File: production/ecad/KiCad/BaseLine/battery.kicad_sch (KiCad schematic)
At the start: 22 parts, among them IC1 AP7362-33SP-13 (3.3V LDO), J3 Conn_01x02, Q3 Si3456DDV, U5 LTC3872ETS8TRMPBF

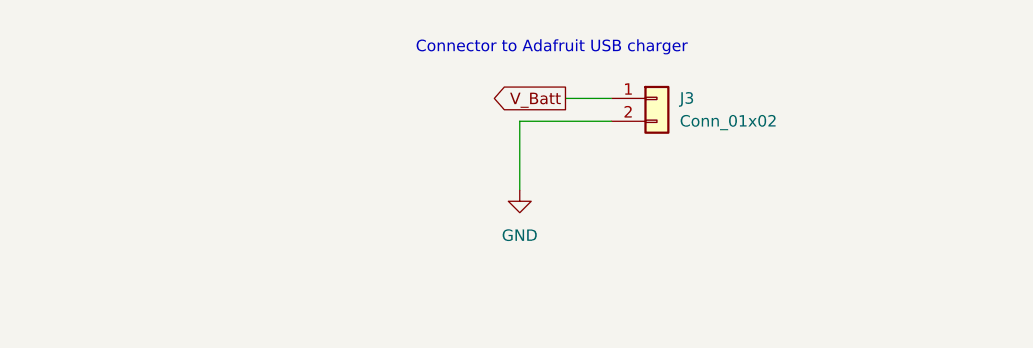
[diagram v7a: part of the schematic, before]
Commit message: Added power switch
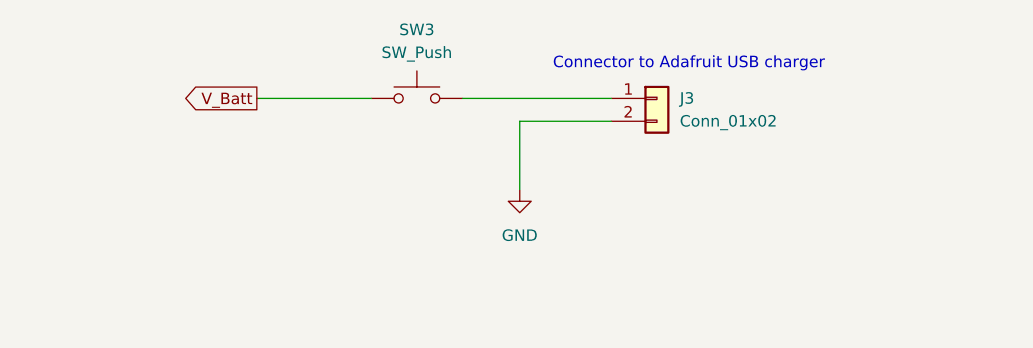
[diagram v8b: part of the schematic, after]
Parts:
- added SW3: SW_Push, symbol Switch:SW_Push
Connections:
- net V_Batt: now also SW3.1; no longer J3.1 (Pin_1)
- new net: J3.1 (Pin_1), SW3.2
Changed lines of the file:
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@@
 	(wire
 		(pts
-			(xy 191.77 35.56) (xy 196.85 35.56)
+			(xy 157.48 35.56) (xy 170.18 35.56)
 		)
 		(stroke
@@
 		(pts
 			(xy 254 134.62) (xy 254 138.43)
+		)
+		(stroke
+			(width 0)
+			(type default)
+		)
+	)
+	(wire
+		(pts
+			(xy 180.34 35.56) (xy 196.85 35.56)
 		)
 		(stroke
@@
 	(text "Connector to Adafruit USB charger"
 		(exclude_from_sim no)
-		(at 190.246 29.972 0)
+		(at 205.486 31.75 0)
 		(effects
 			(font
@@
 	(global_label "V_Batt"
 		(shape output)
-		(at 191.77 35.56 180)
+		(at 157.48 35.56 180)
 		(fields_autoplaced yes)
 		(effects
@@
 		)
 		(property "Intersheetrefs" "${INTERSHEET_REFS}"
-			(at 182.8582 35.56 0)
+			(at 148.5682 35.56 0)
 			(effects
 				(font
@@
 					(unit 1)
 				)
+			)
+		)
+	)
+	(symbol
+		(lib_id "Switch:SW_Push")
+		(at 175.26 35.56 0)
+		(unit 1)
+		(exclude_from_sim no)
+		(in_bom yes)
+		(on_board yes)
+		(dnp no)
+		(fields_autoplaced yes)
+		(property "Reference" "SW3"
+			(at 175.26 27.94 0)
+			(effects
+				(font
+					(size 1.27 1.27)
+				)
+			)
+		)
+		(property "Value" "SW_Push"
+			(at 175.26 30.48 0)
+			(effects
+				(font
+					(size 1.27 1.27)
+				)
+			)
+		)
+		(property "Footprint" ""
+			(at 175.26 30.48 0)
+			(effects
+				(font
+					(size 1.27 1.27)
+				)
+				(hide yes)
+			)
+		)
+		(property "Datasheet" "~"
+			(at 175.26 30.48 0)
+			(effects
+				(font
+					(size 1.27 1.27)
+				)
+				(hide yes)
+			)
+		)
+		(property "Description" "Push button switch, generic, two pins"
+			(at 175.26 35.56 0)
+			(effects
+				(font
+					(size 1.27 1.27)
+				)
+				(hide yes)
+			)
+		)
+		(pin "1"
+		)
+		(pin "2"
+		)
+		(instances
+			(project ""
+				(path "/ba9eda21-3882-41e1-8265-3d8ac781da20/31f727a4-3278-43bf-88f9-c0e8e93f0a52"
+					(reference "SW3")
+					(unit 1)
+				)
